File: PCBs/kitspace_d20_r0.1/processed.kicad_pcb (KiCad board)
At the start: 4 copper layers, 39.2 x 31 mm, 91 parts, among them J1 Conn_01x03, J2 Conn_01x06_Shielded, J3 Conn_01x06_Shielded, J4 Conn_01x06_Shielded, J5 Conn_01x06_Shielded, J6 Conn_02x05_Odd_Even, J7 USB_C_Receptacle_USB2.0, SW1 SW_Push, U1 LTC4367, U10 NC7WZ17, U11 NC7WZ17, U12 NC7WZ17, U13 NC7WZ17, U14 NC7WZ17, U15 NC7WZ17, U16 NC7WZ17, U17 BMX160, U18 AT25SF081, U19 LTC4413-2, U2 AON7804, U3 TPS62135, U4 TPS561201, U5 NP115-2.5, U6 NP115-1.2, U7 ATSAMD51G19A, U8 ICE40UP5K-SG48ITR, U9 NC7WZ17, Y1 32.768kHz

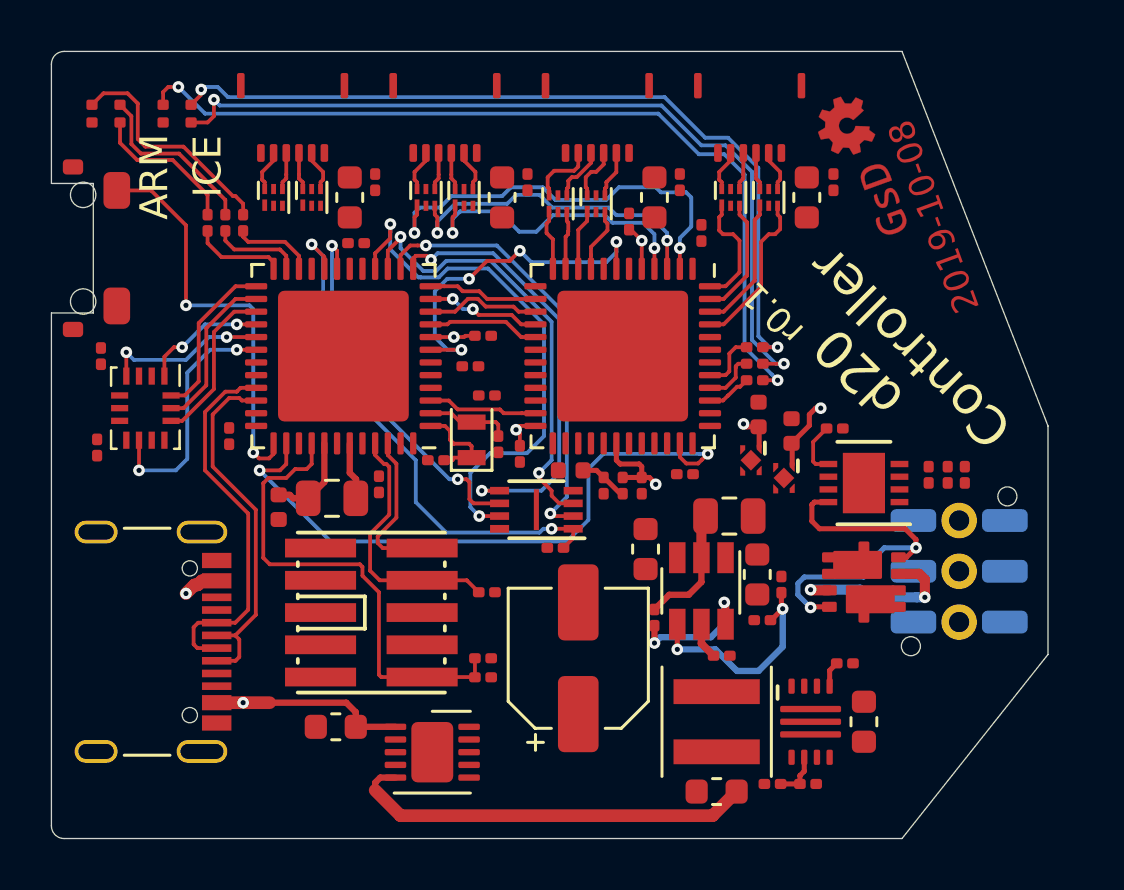
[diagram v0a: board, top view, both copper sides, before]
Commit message: recheck all circuits and clean up fill zone by rerouting the nets using freerouting and manually
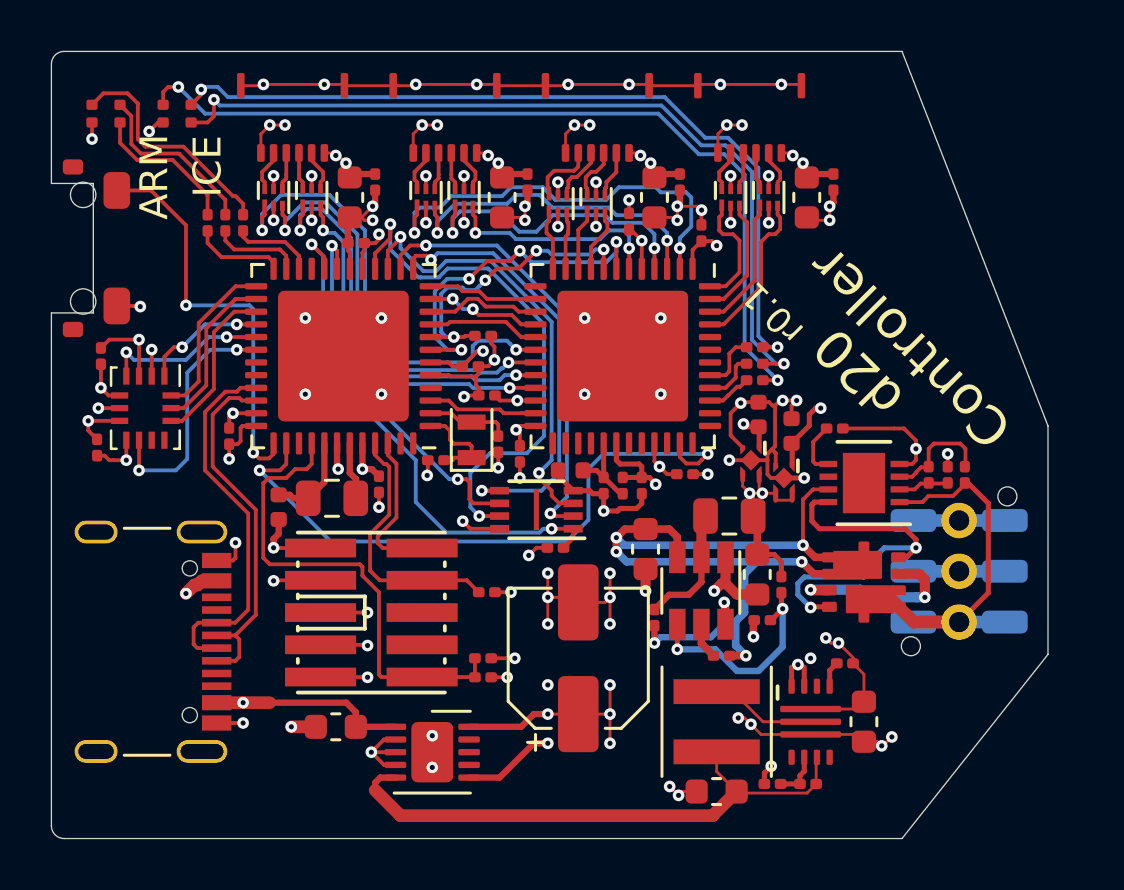
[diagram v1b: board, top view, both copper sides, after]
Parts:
- removed G***: LOGO, oshw_small
- removed G***: LOGO, gsd_logo_small
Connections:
- C1 pad 1: (no net) -> pp_batt_prot
- C1 pad 2: (no net) -> gnd
- C10 pad 1: (no net) -> 3v3
- C10 pad 2: (no net) -> gnd
- C11 pad 1: (no net) -> 3v3
- C11 pad 2: (no net) -> gnd
- C12 pad 1: (no net) -> 3v3
- C12 pad 2: (no net) -> gnd
- C13 pad 1: (no net) -> 3v3
- C13 pad 2: (no net) -> gnd
- C14 pad 2: (no net) -> gnd
- C15 pad 2: (no net) -> gnd
- C16 pad 2: (no net) -> gnd
- C17 pad 1: (no net) -> 3v3
- C17 pad 2: (no net) -> gnd
- C18 pad 1: (no net) -> 3v3
- C18 pad 2: (no net) -> gnd
- C19 pad 1: (no net) -> 3v3
- C19 pad 2: (no net) -> gnd
- C2 pad 2: (no net) -> gnd
- C20 pad 2: (no net) -> gnd
- C21 pad 2: (no net) -> gnd
- C22 pad 2: (no net) -> gnd
- C23 pad 2: (no net) -> gnd
- C24 pad 1: (no net) -> 4v5
- C24 pad 2: (no net) -> gnd
- C25 pad 1: (no net) -> 4v5
- C25 pad 2: (no net) -> gnd
- C26 pad 1: (no net) -> 4v5
- C26 pad 2: (no net) -> gnd
- C27 pad 1: (no net) -> 4v5
- C27 pad 2: (no net) -> gnd
- C28 pad 1: (no net) -> 4v5
- C28 pad 2: (no net) -> gnd
- C29 pad 1: (no net) -> 4v5
- C29 pad 2: (no net) -> gnd
- C30 pad 1: (no net) -> 4v5
- C30 pad 2: (no net) -> gnd
- C31 pad 1: (no net) -> 4v5
- C31 pad 2: (no net) -> gnd
- C32 pad 2: (no net) -> gnd
- C33 pad 1: (no net) -> 3v3
- C33 pad 2: (no net) -> gnd
- C34 pad 1: (no net) -> 3v3
- C34 pad 2: (no net) -> gnd
- C35 pad 2: (no net) -> gnd
- C4 pad 1: (no net) -> pp_batt_prot
- C4 pad 2: (no net) -> gnd
- C5 pad 1: (no net) -> 3v3
- C5 pad 2: (no net) -> gnd
- C6 pad 2: (no net) -> gnd
- C7 pad 2: (no net) -> gnd
- C8 pad 2: (no net) -> gnd
- C9 pad 1: (no net) -> 4v5
- C9 pad 2: (no net) -> gnd
- D1 pad 1: (no net) -> 3v3
- D2 pad 1: (no net) -> 3v3
- J1 pad 1: (no net) -> pp_batt
- J1 pad 3: (no net) -> gnd
- J2 pad 1: (no net) -> 4v5
- J2 pad 6: (no net) -> gnd
- J2 pad SH: (no net) -> gnd
- J3 pad 1: (no net) -> 4v5
- J3 pad 6: (no net) -> gnd
- J3 pad SH: (no net) -> gnd
- J4 pad 1: (no net) -> 4v5
- J4 pad 6: (no net) -> gnd
- J4 pad SH: (no net) -> gnd
- J5 pad 1: (no net) -> 4v5
- J5 pad 6: (no net) -> gnd
- J5 pad SH: (no net) -> gnd
- J6 pad 1: (no net) -> gnd
- J6 pad 3: (no net) -> gnd
- J6 pad 5: (no net) -> gnd
- J6 pad 6: (no net) -> swo
- J6 pad 7: (no net) -> gnd
- J6 pad 9: (no net) -> gnd
- J7 pad A1: (no net) -> gnd
- J7 pad A12: (no net) -> gnd
- J7 pad B1: (no net) -> gnd
- J7 pad B12: (no net) -> gnd
- J7 pad S1: (no net) -> gnd
- L1 pad 1: (no net) -> N$7
- L1 pad 2: (no net) -> 4v5_in
- L2 pad 2: (no net) -> 3v3
- R1 pad 2: (no net) -> gnd
- R10 pad 2: (no net) -> gnd
- R17 pad 2: (no net) -> gnd
- R18 pad 2: (no net) -> 3v3
- R19 pad 2: (no net) -> 3v3
- R2 pad 1: (no net) -> N$5
- R2 pad 2: (no net) -> gnd
- R20 pad 2: (no net) -> 3v3
- R3 pad 1: (no net) -> N$4
- R3 pad 2: (no net) -> N$5
- R4 pad 1: (no net) -> pp_batt
- R4 pad 2: (no net) -> N$4
- R5 pad 2: (no net) -> pp_batt_prot
- R6 pad 2: (no net) -> 4v5_in
- R7 pad 2: (no net) -> gnd
- R8 pad 2: (no net) -> pp_batt_prot
- R9 pad 2: (no net) -> 3v3
- SW1 pad 2: (no net) -> gnd
- U1 pad 1: (no net) -> pp_batt
- U1 pad 2: (no net) -> N$5
- U1 pad 3: (no net) -> N$4
- U1 pad 4: (no net) -> gnd
- U1 pad 7: (no net) -> pp_batt_prot
- U10 pad 1: (no net) -> _led0_sclk
- U10 pad 2: (no net) -> gnd
- U10 pad 3: (no net) -> _led0_latch
- U10 pad 5: (no net) -> 4v5
- U11 pad 2: (no net) -> gnd
- U11 pad 3: (no net) -> _led1_data
- U11 pad 5: (no net) -> 4v5
- U12 pad 2: (no net) -> gnd
- U12 pad 5: (no net) -> 4v5
- U13 pad 2: (no net) -> gnd
- U13 pad 5: (no net) -> 4v5
- U14 pad 2: (no net) -> gnd
- U14 pad 5: (no net) -> 4v5
- U15 pad 2: (no net) -> gnd
- U15 pad 5: (no net) -> 4v5
- U16 pad 2: (no net) -> gnd
- U16 pad 5: (no net) -> 4v5
- U17 pad 2: (no net) -> gnd
- U17 pad 3: (no net) -> gnd
- U17 pad 5: (no net) -> 3v3
- U17 pad 6: (no net) -> gnd
- U17 pad 7: (no net) -> gnd
- U17 pad 8: (no net) -> 3v3
- U18 pad 4: (no net) -> gnd
- U18 pad 8: (no net) -> 3v3
- U19 pad 10: (no net) -> 4v5
- U19 pad 11: (no net) -> gnd
- U19 pad 2: (no net) -> gnd
- U19 pad 3: (no net) -> gnd
- U19 pad 4: (no net) -> gnd
- U19 pad 6: (no net) -> 4v5
- U2 pad 1: (no net) -> pp_batt_prot
- U2 pad 4: (no net) -> pp_batt
- U3 pad 1: (no net) -> pp_batt_prot
- U3 pad 10: (no net) -> gnd
- U3 pad 11: (no net) -> gnd
- U3 pad 2: (no net) -> N$7
- U3 pad 3: (no net) -> gnd
- U3 pad 6: (no net) -> 4v5_in
- U4 pad 1: (no net) -> gnd
- U4 pad 3: (no net) -> pp_batt_prot
- U5 pad 2: (no net) -> gnd
- U5 pad 3: (no net) -> 3v3
- U5 pad 4: (no net) -> 3v3
- U6 pad 2: (no net) -> gnd
- U6 pad 3: (no net) -> 3v3
- U6 pad 4: (no net) -> 3v3
- U7 pad 17: (no net) -> 3v3
- U7 pad 18: (no net) -> gnd
- U7 pad 35: (no net) -> gnd
- U7 pad 36: (no net) -> 3v3
- U7 pad 42: (no net) -> gnd
- U7 pad 44: (no net) -> 3v3
- U7 pad 49: (no net) -> gnd
- U7 pad 5: (no net) -> gnd
- U7 pad 6: (no net) -> 3v3
- U8 pad 1: (no net) -> 3v3
- U8 pad 18: (no net) -> _led0_sclk
- U8 pad 19: (no net) -> _led0_latch
- U8 pad 20: (no net) -> _led0_blank
- U8 pad 21: (no net) -> _led0_data
- U8 pad 22: (no net) -> 3v3
- U8 pad 29: (no net) -> 1v2_pll
- U8 pad 33: (no net) -> 3v3
- U8 pad 49: (no net) -> gnd
- U8 pad 6: (no net) -> _led1_data
- U8 pad 8: (no net) -> ice_config_reset
- U9 pad 1: (no net) -> _led0_blank
- U9 pad 2: (no net) -> gnd
- U9 pad 3: (no net) -> _led0_data
- U9 pad 5: (no net) -> 4v5
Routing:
- net gnd: track 0.00 -> 284.6 mm, vias 0 -> 94
- net 3v3: track 0.00 -> 118.5 mm, vias 0 -> 17
- net 4v5: track 0.00 -> 80.8 mm, vias 0 -> 22
- net pp_batt_prot: track 0.00 -> 40.7 mm, vias 0 -> 7
- net _led0_sclk: track 0.00 -> 18.7 mm, vias 0 -> 2
- net pp_batt: track 0.00 -> 18.5 mm
- net _led0_latch: track 0.00 -> 16.9 mm, vias 0 -> 2
- net _led0_blank: track 0.00 -> 16.3 mm, vias 0 -> 2
- net _led0_data: track 0.00 -> 14.2 mm, vias 0 -> 2
- net ice_config_reset: track 1.76 -> 12.0 mm, vias 1 -> 4
- net _led1_data: track 0.00 -> 8.85 mm, vias 0 -> 2
- net 4v5_in: track 16.2 -> 22.5 mm
- net N$4: track 0.00 -> 4.40 mm
- net N$7: track 0.00 -> 4.19 mm
- net (no net): track 0.00 -> 3.60 mm
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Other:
- board text removed: "2019-10-08"
